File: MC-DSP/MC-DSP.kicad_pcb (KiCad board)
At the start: 6 copper layers, 160 x 100 mm, 165 parts, among them J1 374385, J80 5-1634513-1, J81 5-1634513-1, J82 5-1634513-1, SW1 SW_SPDT, T1 ERRORSTS, U1 TMS320F28388DZWT, U10 ECS-2520MV-xxx-xx, U12 BU4831F-TR, U13 BU4811G-TR, U2 SBH41-NBPB-D10-ST-BK, U20 R-78E3.3-1.0, U200 FT2232HL, U201 TPD2S017, U202 USB_B, U203 AZ1117-3.3, U204 ISO7730DW, U205 ISO7730DW, U206 ISO7730DW, U207 Crystal_GND24, U21 R-78B1.2-2.0, U60 OPA365xxD, U61 OPA365xxD, U62 OPA365xxD, U63 OPA365xxD, U64 OPA365xxD, U65 MAX6126AASA, U80 OPA365xxD, U81 OPA365xxD, U82 OPA365xxD

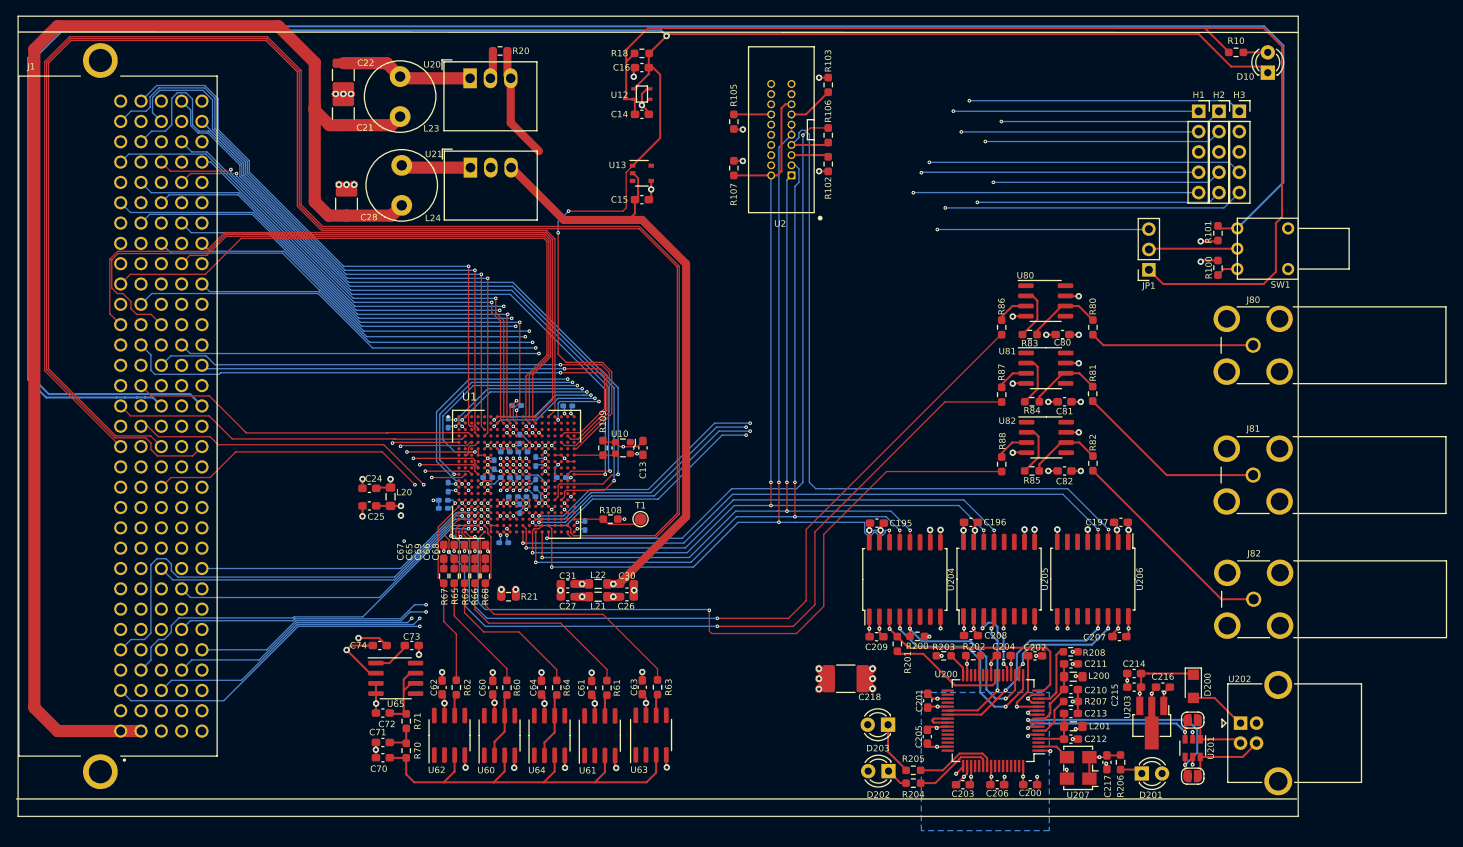
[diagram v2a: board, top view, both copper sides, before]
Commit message: Added labels on the silkscreen
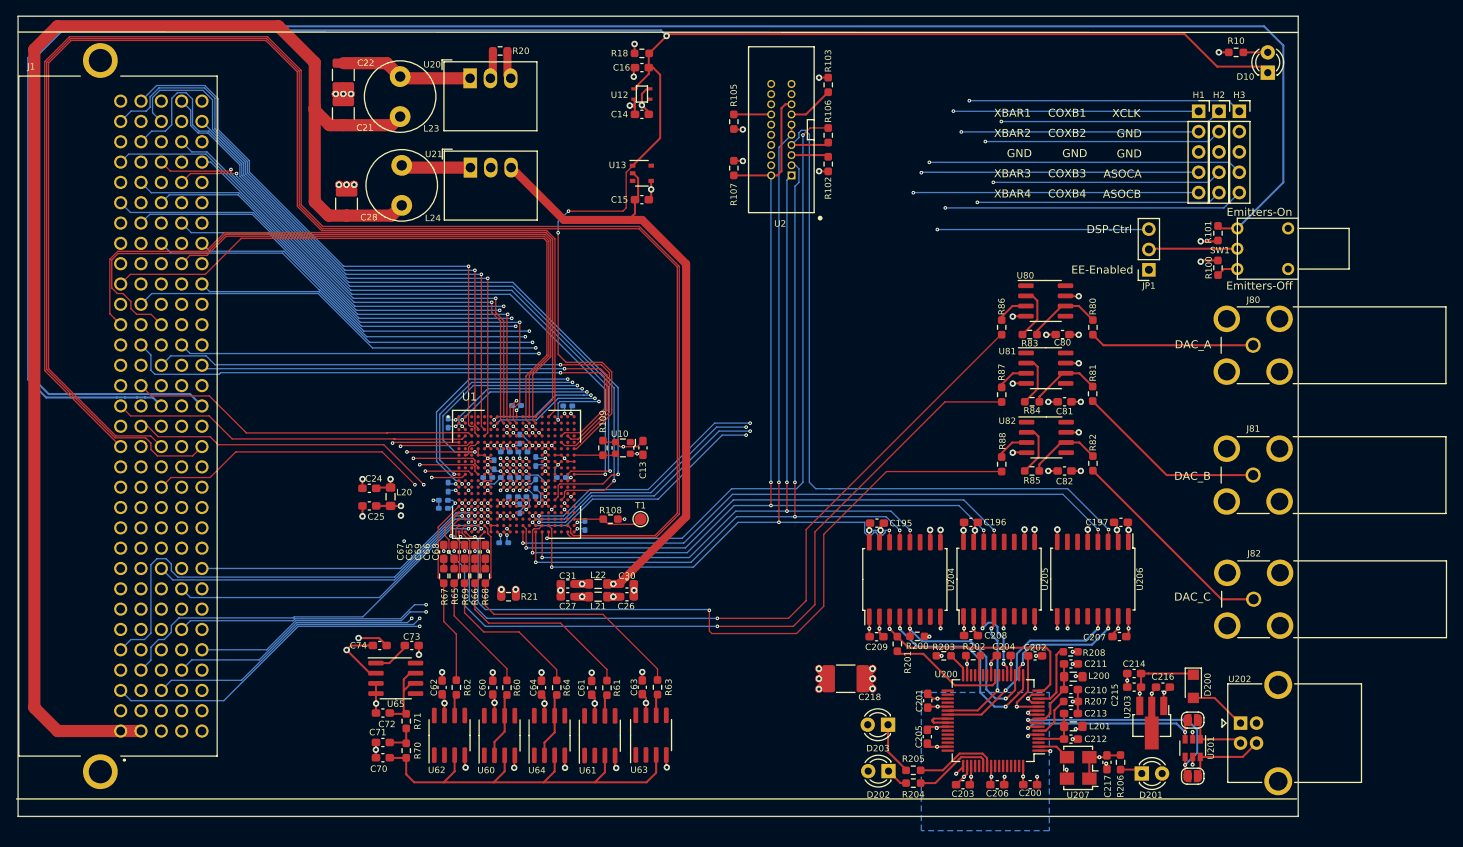
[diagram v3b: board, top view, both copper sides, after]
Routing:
- net +3V3: track 187.3 -> 37.1 mm, vias 17 -> 20
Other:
- board text added: "ASOCA"
- board text added: "ASOCB"
- board text added: "COXB1"
- board text added: "COXB2"
- board text added: "COXB3"
- board text added: "COXB4"
- board text added: "DAC_A"
- board text added: "DAC_B"
- board text added: "DAC_C"
- board text added: "DSP-Ctrl"
- board text added: "EE-Enabled"
- board text added: "Emitters-Off"
- board text added: "Emitters-On"
- board text added: "GND"
- board text added: "XBAR1"
- board text added: "XBAR2"
- board text added: "XBAR3"
- board text added: "XBAR4"
- board text added: "XCLK"
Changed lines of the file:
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@@
   (general
     (thickness 1.6)
-    (drawings 6)
-    (tracks 2362)
+    (drawings 28)
+    (tracks 2358)
     (zones 0)
     (modules 165)
@@
   (module mark_footprints:GT12MABE (layer F.Cu)
     (at 253.5 40.8 180)
-    (fp_text reference SW1 (at -5.4 -4.5) (layer F.SilkS)
+    (fp_text reference SW1 (at 2.18 -0.2) (layer F.SilkS)
       (effects (font (size 0.8 0.8) (thickness 0.2)))
     )
@@
     )
   )
+  (gr_text DAC_C (at 247.89 84.32) (layer F.SilkS)
+    (effects (font (size 1 1) (thickness 0.15)))
+  )
+  (gr_text DAC_B (at 247.89 69.23) (layer F.SilkS)
+    (effects (font (size 1 1) (thickness 0.15)))
+  )
+  (gr_text DAC_A (at 247.961429 52.78) (layer F.SilkS)
+    (effects (font (size 1 1) (thickness 0.15)))
+  )
+  (gr_text Emitters-Off (at 256.26 45.44) (layer F.SilkS)
+    (effects (font (size 1 1) (thickness 0.15)))
+  )
+  (gr_text Emitters-On (at 256.26 36.23) (layer F.SilkS)
+    (effects (font (size 1 1) (thickness 0.15)))
+  )
+  (gr_text EE-Enabled (at 236.62 43.44) (layer F.SilkS)
+    (effects (font (size 1 1) (thickness 0.15)))
+  )
+  (gr_text DSP-Ctrl (at 237.49 38.38) (layer F.SilkS)
+    (effects (font (size 1 1) (thickness 0.15)))
+  )
+  (gr_text XBAR4 (at 225.4 33.93) (layer F.SilkS)
+    (effects (font (size 1 1) (thickness 0.15)))
+  )
+  (gr_text XBAR3 (at 225.4 31.4075) (layer F.SilkS)
+    (effects (font (size 1 1) (thickness 0.15)))
+  )
+  (gr_text XBAR2 (at 225.4 26.3625) (layer F.SilkS)
+    (effects (font (size 1 1) (thickness 0.15)))
+  )
+  (gr_text XBAR1 (at 225.4 23.84) (layer F.SilkS)
+    (effects (font (size 1 1) (thickness 0.15)))
+  )
+  (gr_text "COXB4\n" (at 232.23 33.93) (layer F.SilkS)
+    (effects (font (size 1 1) (thickness 0.15)))
+  )
+  (gr_text "COXB1\n" (at 232.23 23.84) (layer F.SilkS)
+    (effects (font (size 1 1) (thickness 0.15)))
+  )
+  (gr_text "COXB2\n" (at 232.23 26.3625) (layer F.SilkS)
+    (effects (font (size 1 1) (thickness 0.15)))
+  )
+  (gr_text "COXB3\n" (at 232.23 31.4075) (layer F.SilkS)
+    (effects (font (size 1 1) (thickness 0.15)))
+  )
+  (gr_text ASOCB (at 239.082381 33.97) (layer F.SilkS)
+    (effects (font (size 1 1) (thickness 0.15)))
+  )
+  (gr_text ASOCA (at 239.15381 31.4475) (layer F.SilkS)
+    (effects (font (size 1 1) (thickness 0.15)))
+  )
+  (gr_text GND (at 226.257143 28.885) (layer F.SilkS)
+    (effects (font (size 1 1) (thickness 0.15)))
+  )
+  (gr_text GND (at 233.182381 28.885) (layer F.SilkS)
+    (effects (font (size 1 1) (thickness 0.15)))
+  )
+  (gr_text GND (at 239.987143 28.925) (layer F.SilkS)
+    (effects (font (size 1 1) (thickness 0.15)))
+  )
+  (gr_text "GND\n" (at 239.987143 26.4025) (layer F.SilkS)
+    (effects (font (size 1 1) (thickness 0.15)))
+  )
+  (gr_text "XCLK\n" (at 239.63 23.88) (layer F.SilkS)
+    (effects (font (size 1 1) (thickness 0.15)))
+  )
   (gr_line (start 261.112 13.7668) (end 101.092 13.716) (layer F.SilkS) (width 0.12))
   (gr_line (start 260.912 109.5772) (end 100.892 109.5772) (layer F.SilkS) (width 0.12))
@@
   (gr_line (start 261.112 11.7348) (end 101.092 11.7348) (layer Edge.Cuts) (width 0.05))
   (gr_line (start 261.112 111.76) (end 261.112 11.7348) (layer Edge.Cuts) (width 0.05))
+  (via (at 251.19 16.25) (size 0.8128) (drill 0.4064) (layers F.Cu B.Cu) (net 2))
   (via (at 168.6 62.2) (size 0.45) (drill 0.2) (layers F.Cu B.Cu) (net 29))
   (via (at 156.6 70.2) (size 0.45) (drill 0.2) (layers F.Cu B.Cu) (net 40))
@@
   (via (at 201.215 31.106) (size 0.8) (drill 0.4) (layers F.Cu B.Cu) (net 2))
   (via (at 191.69 25.899) (size 0.8) (drill 0.4) (layers F.Cu B.Cu) (net 2))
-  (segment (start 178.1575 24.053) (end 178.2075 24.003) (width 0.254) (layer F.Cu) (net 2))
-  (segment (start 178.181 23.5955) (end 178.181 22.225) (width 0.254) (layer F.Cu) (net 2))
+  (segment (start 178.1575 24.053) (end 178.19025 24.02025) (width 0.254) (layer F.Cu) (net 2))
   (segment (start 190.6255 25.899) (end 190.559 25.8325) (width 0.254) (layer F.Cu) (net 2))
   (segment (start 191.69 25.899) (end 190.6255 25.899) (width 0.254) (layer F.Cu) (net 2))
@@
   (segment (start 201.2295 19.4075) (end 201.215 19.422) (width 0.254) (layer F.Cu) (net 2))
   (segment (start 202.359 19.4075) (end 201.2295 19.4075) (width 0.254) (layer F.Cu) (net 2))
-  (segment (start 177.11101 21.80099) (end 176.799 22.113) (width 0.254) (layer F.Cu) (net 2))
-  (segment (start 177.11101 17.42949) (end 177.11101 21.80099) (width 0.254) (layer F.Cu) (net 2))
-  (segment (start 178.1575 16.383) (end 177.11101 17.42949) (width 0.254) (layer F.Cu) (net 2))
-  (segment (start 178.445 22.113) (end 176.799 22.113) (width 0.254) (layer F.Cu) (net 2))
-  (segment (start 252.429 16.209) (end 252.429 16.256) (width 0.254) (layer F.Cu) (net 2))
-  (segment (start 249.428 13.208) (end 252.429 16.209) (width 0.254) (layer F.Cu) (net 2))
-  (segment (start 179.832 13.208) (end 249.428 13.208) (width 0.254) (layer F.Cu) (net 2))
-  (segment (start 177.11101 15.92899) (end 179.832 13.208) (width 0.254) (layer F.Cu) (net 2))
-  (segment (start 177.11101 17.42949) (end 177.11101 15.92899) (width 0.254) (layer F.Cu) (net 2))
-  (segment (start 244.221 45.212) (end 242.443 43.434) (width 0.254) (layer F.Cu) (net 2))
-  (segment (start 256.794 45.212) (end 244.221 45.212) (width 0.254) (layer F.Cu) (net 2))
-  (segment (start 258.318 37.592) (end 258.318 43.688) (width 0.254) (layer F.Cu) (net 2))
-  (segment (start 259.08 36.83) (end 258.318 37.592) (width 0.254) (layer F.Cu) (net 2))
-  (segment (start 259.08 15.494) (end 259.08 36.83) (width 0.254) (layer F.Cu) (net 2))
-  (segment (start 258.318 43.688) (end 256.794 45.212) (width 0.254) (layer F.Cu) (net 2))
-  (segment (start 256.794 13.208) (end 259.08 15.494) (width 0.254) (layer F.Cu) (net 2))
-  (segment (start 249.428 13.208) (end 256.794 13.208) (width 0.254) (layer F.Cu) (net 2))
+  (segment (start 178.1575 16.383) (end 178.1575 16.383) (width 0.254) (layer F.Cu) (net 2))
   (via (at 233.68 46.736) (size 0.8) (drill 0.4) (layers F.Cu B.Cu) (net 2))
   (via (at 233.68 55.118) (size 0.8) (drill 0.4) (layers F.Cu B.Cu) (net 2))
@@
   (segment (start 162.2625 19.0843) (end 162.6746 19.4964) (width 1.016) (layer F.Cu) (net 2))
   (segment (start 162.2625 16.081) (end 162.2625 19.0843) (width 1.016) (layer F.Cu) (net 2))
-  (segment (start 162.6746 25.0746) (end 162.6746 19.4964) (width 1.016) (layer F.Cu) (net 2))
-  (segment (start 166.2 28.6) (end 162.6746 25.0746) (width 1.016) (layer F.Cu) (net 2))
   (segment (start 147.65 70.65) (end 145.9625 70.65) (width 0.254) (layer F.Cu) (net 2))
   (via (at 147.65 69.6) (size 0.8128) (drill 0.4064) (layers F.Cu B.Cu) (net 2))
@@
   (segment (start 181.356 26.973) (end 181.356 19.047) (width 0.254) (layer F.Cu) (net 4))
   (segment (start 177.91 30.419) (end 181.356 26.973) (width 0.254) (layer F.Cu) (net 4))
-  (segment (start 182.3955 13.97) (end 182.15775 14.20775) (width 0.254) (layer F.Cu) (net 4))
-  (segment (start 248.666 13.97) (end 182.3955 13.97) (width 0.254) (layer F.Cu) (net 4))
-  (segment (start 252.73 18.034) (end 248.666 13.97) (width 0.254) (layer F.Cu) (net 4))
-  (segment (start 256.54 18.034) (end 252.73 18.034) (width 0.254) (layer F.Cu) (net 4))
-  (segment (start 257.302 18.796) (end 256.54 18.034) (width 0.254) (layer F.Cu) (net 4))
   (segment (start 182.15775 14.20775) (end 179.9825 16.383) (width 0.254) (layer F.Cu) (net 4))
   (via (at 182.15775 14.20775) (size 0.8128) (drill 0.4064) (layers F.Cu B.Cu) (net 4))
@@
   (segment (start 230.7855 51.53) (end 229.648 51.53) (width 0.254) (layer F.Cu) (net 2))
   (segment (start 229.87 68.58) (end 231.0395 68.58) (width 0.254) (layer F.Cu) (net 2))
+  (via (at 178.15 15.21) (size 0.8128) (drill 0.4064) (layers F.Cu B.Cu) (net 2))
+  (segment (start 178.19025 24.02025) (end 178.2075 24.003) (width 0.254) (layer F.Cu) (net 2))
+  (via (at 177.56 22.91) (size 0.8128) (drill 0.4064) (layers F.Cu B.Cu) (net 2))
+  (segment (start 178.181 22.709) (end 178.181 22.225) (width 0.254) (layer F.Cu) (net 2))
+  (segment (start 177.98 22.91) (end 178.181 22.709) (width 0.254) (layer F.Cu) (net 2))
+  (segment (start 177.56 22.91) (end 177.98 22.91) (width 0.254) (layer F.Cu) (net 2))
+  (segment (start 177.98 22.948) (end 178.181 23.149) (width 0.254) (layer F.Cu) (net 2))
+  (segment (start 177.98 22.91) (end 177.98 22.948) (width 0.254) (layer F.Cu) (net 2))
+  (segment (start 178.181 23.149) (end 178.181 23.5955) (width 0.254) (layer F.Cu) (net 2))
+  (segment (start 178.181 22.225) (end 178.181 23.149) (width 0.254) (layer F.Cu) (net 2))
+  (segment (start 178.15 16.3755) (end 178.1575 16.383) (width 0.254) (layer F.Cu) (net 2))
+  (segment (start 178.15 15.21) (end 178.15 16.3755) (width 0.254) (layer F.Cu) (net 2))
+  (segment (start 252.423 16.25) (end 252.429 16.256) (width 0.254) (layer F.Cu) (net 2))
+  (segment (start 251.19 16.25) (end 252.423 16.25) (width 0.254) (layer F.Cu) (net 2))
+  (segment (start 182.3955 13.97) (end 182.15775 14.20775) (width 0.254) (layer F.Cu) (net 4))
+  (segment (start 246.91 13.97) (end 182.3955 13.97) (width 0.254) (layer F.Cu) (net 4))
+  (segment (start 250.974 18.034) (end 246.91 13.97) (width 0.254) (layer F.Cu) (net 4))
+  (segment (start 256.54 18.034) (end 250.974 18.034) (width 0.254) (layer F.Cu) (net 4))
+  (segment (start 257.302 18.796) (end 256.54 18.034) (width 0.254) (layer F.Cu) (net 4))
   (segment (start 156.211221 72.138779) (end 155.75 72.6) (width 0.254) (layer In2.Cu) (net 7))
   (segment (start 159.338779 72.138779) (end 156.211221 72.138779) (width 0.254) (layer In2.Cu) (net 7))
@@
       (pts
         (xy 285.1 5.2) (xy 285.2 91.6) (xy 243.1 92) (xy 242.5 81) (xy 204.1 80.5)
-        (xy 203.8 116.9) (xy 186.7 116.4) (xy 186.8 85.2) (xy 173.74 85.2) (xy 173.75 58.8)
+        (xy 203.8 116.9) (xy 186.89 116.4) (xy 186.8 85.2) (xy 173.74 85.2) (xy 173.75 58.8)
         (xy 153.11 58.79) (xy 153.05 71.87) (xy 142.99 71.86) (xy 143 5.05)
       )
